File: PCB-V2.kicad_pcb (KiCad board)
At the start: 4 copper layers, 96.7 x 78.4 mm, 33 parts, among them J1 TB010-508-02BE, J2 TB010-508-02BE, J3 TB004-508-03BE, J4 TB004-508-03BE, U2 *, U3 6N137, U4 6N137, U5 *, U6 MC78M05CTG

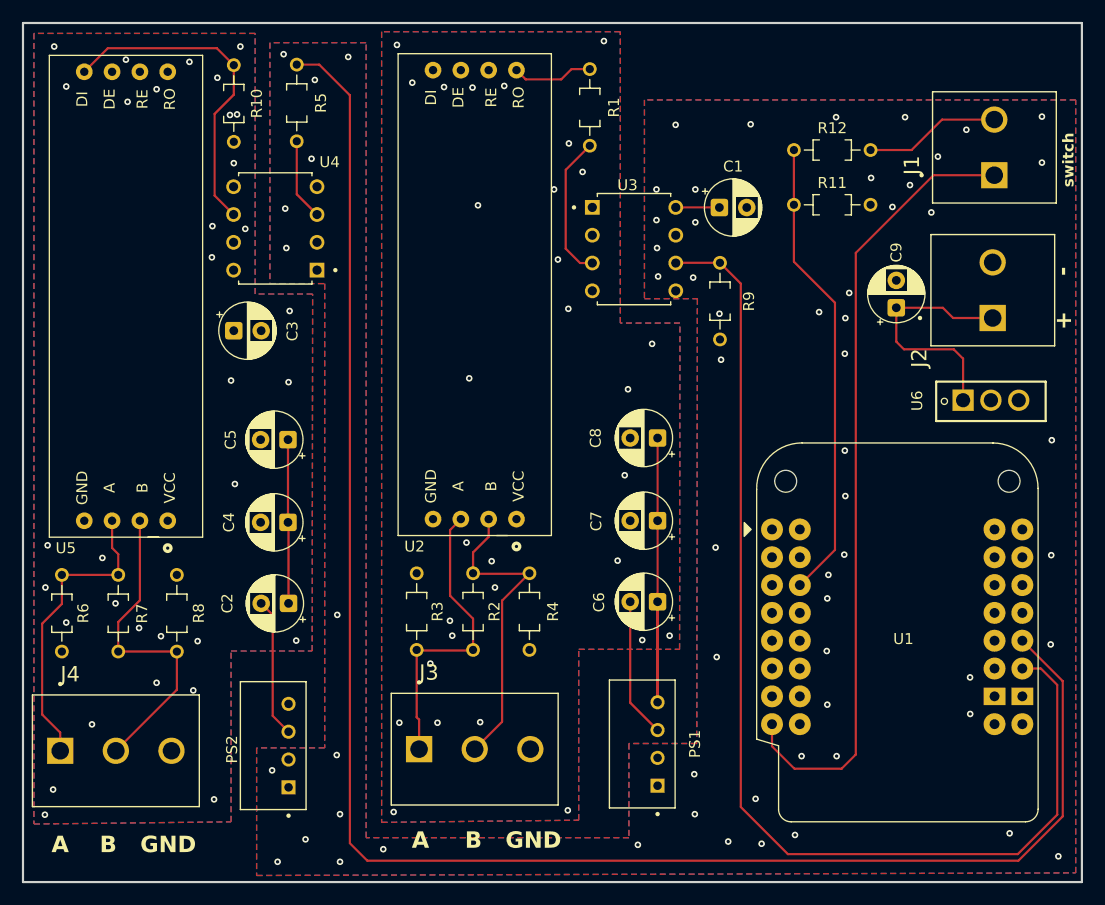
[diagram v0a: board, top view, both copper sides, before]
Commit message: upgrade to more robust switch network
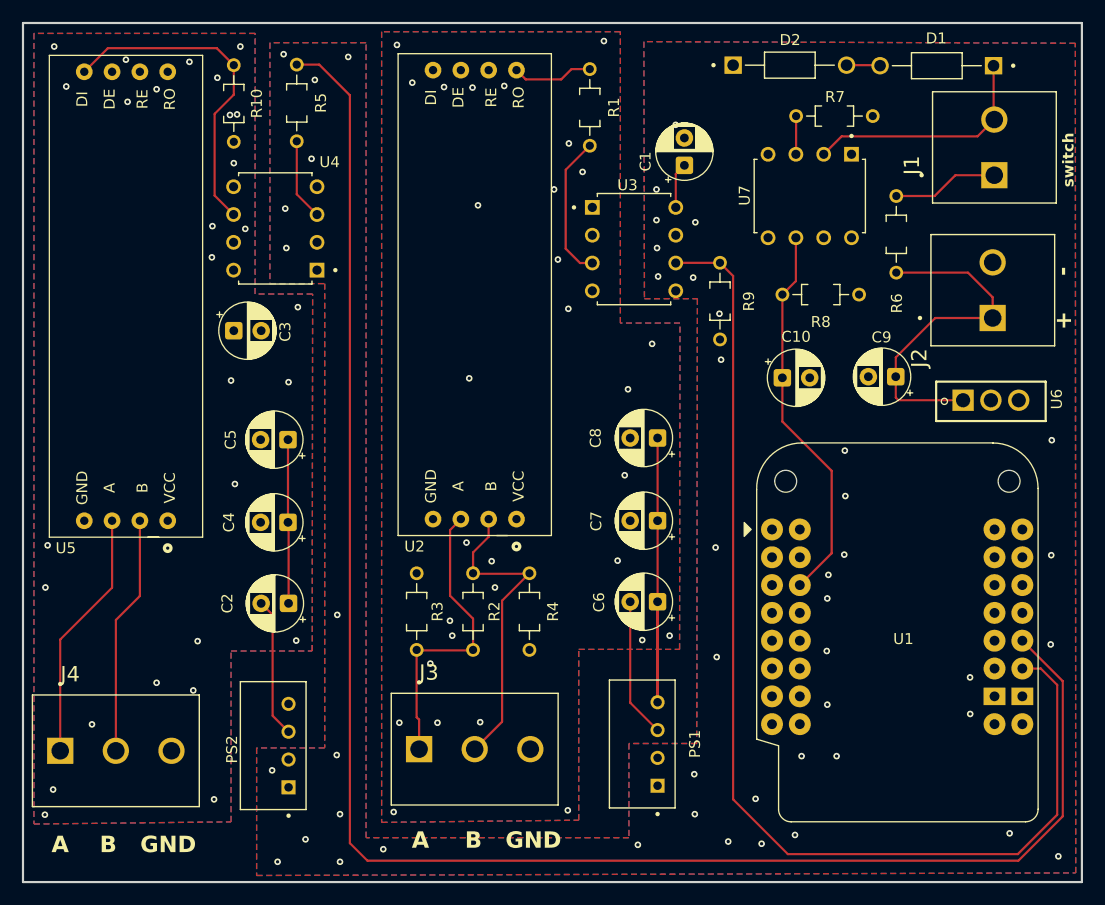
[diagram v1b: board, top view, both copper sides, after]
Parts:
- removed R11: R4k7, dmx_interceptor:R_THT
- removed R12: R30, dmx_interceptor:R_THT
- added C10: C100n, Capacitor_THT:CP_Radial_D5.0mm_P2.50mm, F.Cu at (118.0, 142.4)
- added D1: 1N4742A, dmx_interceptor:DIOAD1036W78L463D237, F.Cu at (132.1, 113.9)
- added D2: 1N4742A, dmx_interceptor:DIOAD1036W78L463D237, F.Cu at (118.7, 113.8)
- added U7: 6N137, dmx_interceptor:DIP762W50P254L1016H465Q8, F.Cu at (120.5, 125.8)
- R5: value R74 -> R470
- R6: value R562 -> R2k2
- R7: value R133 -> R100
- R8: value R562 -> R10k
- U6: value MC78M05CTG -> LM1117T 3,3V
- moved R6 83.7 mm to (128.4, 129.3)
- moved R7 79.6 mm to (122.8, 118.5), turned to 180 degrees
- moved R8 65.6 mm to (121.5, 134.8), turned to 0 degrees
- moved C9 6.30 mm to (128.3, 142.3), turned to 180 degrees
- moved C1 5.00 mm to (109.0, 123.0), turned to 90 degrees
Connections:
- C9 pad 1: Net-(U6-IN) -> +VDC9
- J2 pad 1: Net-(U6-IN) -> +VDC9
- R6 pad 1: +VDC3 -> +VDC9
- R6 pad 2: Net-(U5-A) -> Net-(J1-Pad1)
- R7 pad 1: Net-(U5-A) -> GND1
- R7 pad 2: Net-(U5-B) -> Net-(U7-C)
- R8 pad 1: Net-(U5-B) -> Net-(U7-VO)
- R8 pad 2: GND3 -> +VDC1
- U1 pad 3V3: Net-(J1-Pad1) -> unconnected-(U1-Pad3V3)
- U1 pad 5: Net-(R11-Pad1) -> Net-(U7-VO)
- U6 pad 1: Net-(U6-IN) -> +VDC9
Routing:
- net Net-(J1-Pad1): track 72.4 -> 9.74 mm
- net Net-(R11-Pad1): track 42.6 -> 0.00 mm
- net Net-(U7-VO): track 0.00 -> 35.3 mm
- net +VDC9: track 0.00 -> 32.9 mm
- net Net-(U6-IN): track 23.8 -> 0.00 mm
- net Net-(U7-A): track 12.5 -> 21.8 mm
- net Net-(U5-B): track 29.5 -> 21.9 mm
- net Net-(U5-A): track 27.8 -> 23.0 mm
- net Net-(U7-C): track 0.00 -> 3.50 mm
- net Net-(D1-Pad2): track 0.00 -> 3.08 mm
- net GND3: vias 33 -> 28
- net GND1: vias 64 -> 48

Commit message: more robustness in switch pin
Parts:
- removed D2: 1N4742A, dmx_interceptor:DIOAD1036W78L463D237
- added C11: C100n, Capacitor_THT:CP_Radial_D5.0mm_P2.50mm, F.Cu at (135.2, 114.4)
- added R11: R100k, dmx_interceptor:R_THT, F.Cu at (125.8, 116.2)
- D1: value 1N4742A -> 1,5KE12A; footprint dmx_interceptor:DIOAD1036W78L463D237 -> dmx_interceptor:DIOAD1586W101L900D530
- moved D1 18.6 mm to (114.8, 120.9), turned to -90 degrees
- moved R6 16.5 mm to (125.8, 113.0), turned to 0 degrees
- moved U7 3.83 mm to (124.3, 126.3)
- moved R7 3.11 mm to (125.8, 119.1)
- moved J1 0.21 mm to (137.2, 124.0)
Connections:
- J1 pad 1: Net-(J1-Pad1) -> +VDC9
- J1 pad 2: Net-(U7-A) -> Net-(J1-Pad2)
- R6 pad 1: +VDC9 -> Net-(U7-A)
- R6 pad 2: Net-(J1-Pad1) -> Net-(J1-Pad2)
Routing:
- net Net-(U7-A): track 21.8 -> 33.9 mm
- net Net-(J1-Pad2): track 0.00 -> 10.4 mm
- net Net-(J1-Pad1): track 9.74 -> 0.00 mm
- net +VDC9: track 32.9 -> 36.9 mm
- net Net-(D1-Pad2): track 3.08 -> 0.00 mm
- net Net-(U7-VO): track 35.3 -> 36.6 mm
